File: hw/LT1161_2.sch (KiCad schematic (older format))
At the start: 7 parts, among them U501 MOSFET_DRIVER_LT1161, U502 MOSFET_IPG20N04S4L11ATMA1, U503 MOSFET_IPG20N04S4L11ATMA1

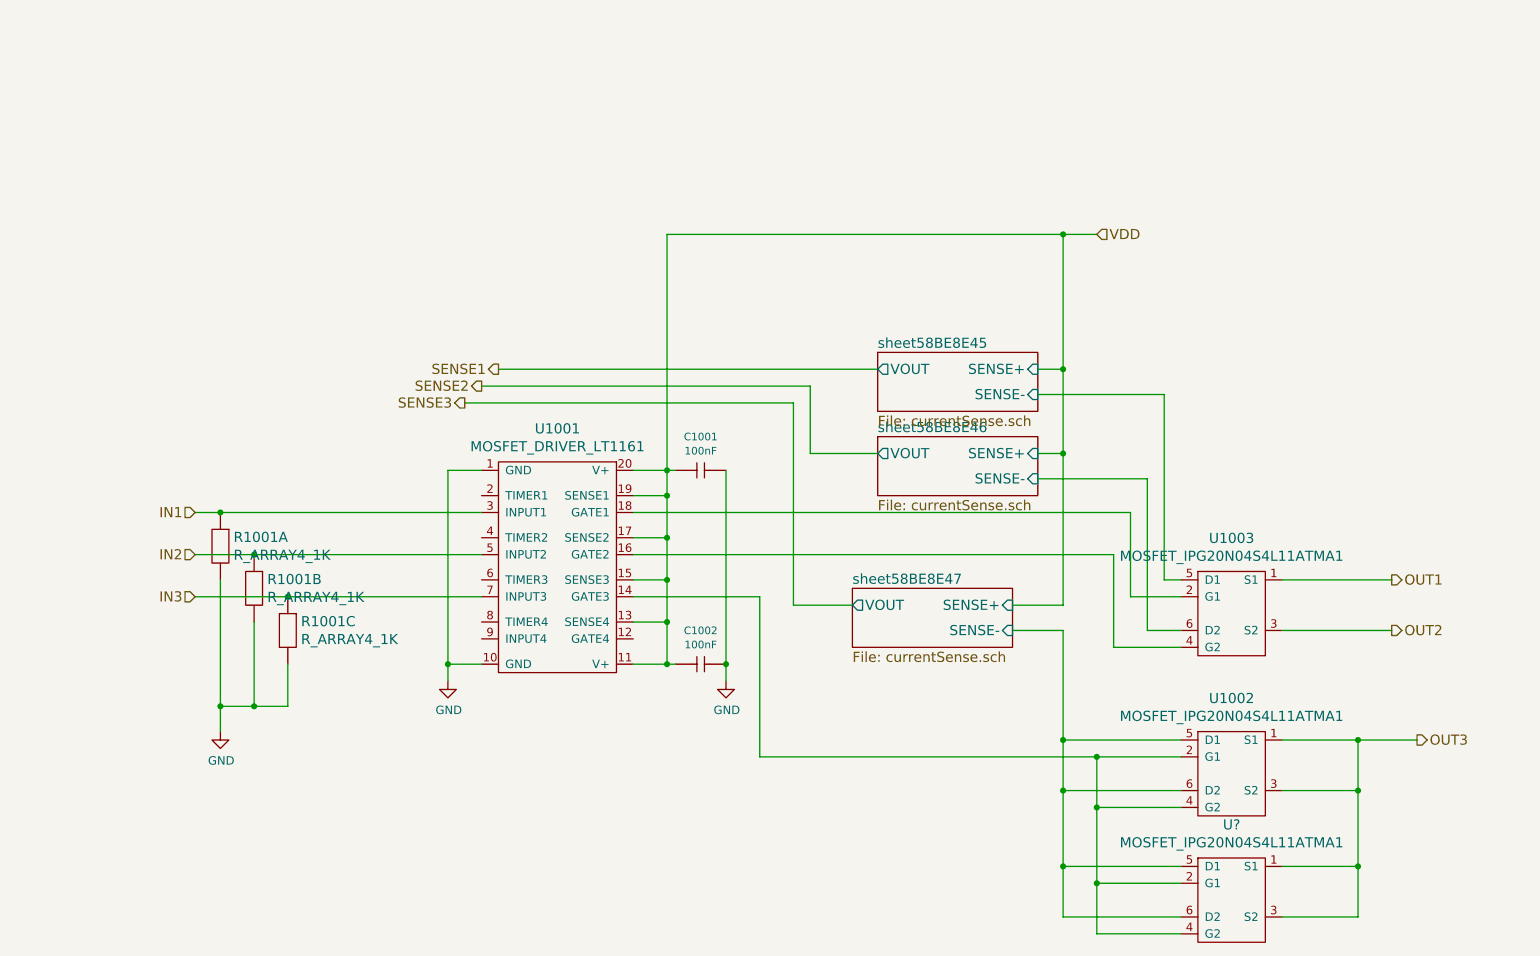
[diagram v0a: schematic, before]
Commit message: first pcb revision ready to order
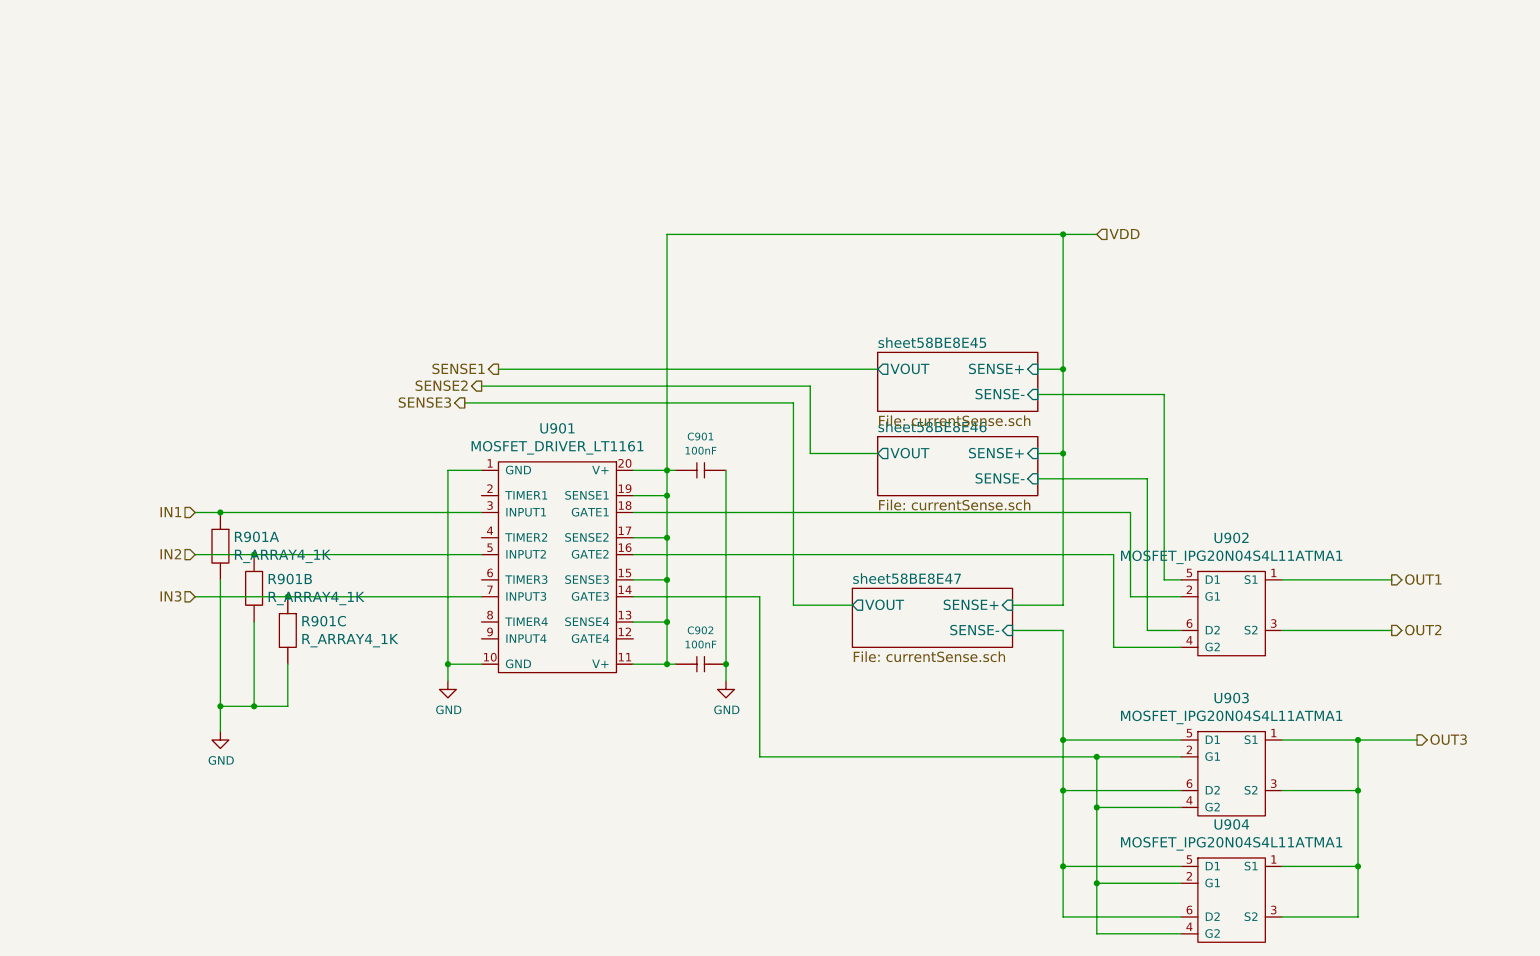
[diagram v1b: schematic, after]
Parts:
- removed C501, C502: 100nF, kemet:0603, symbol 100nF
- removed R501: R_ARRAY4_1K, usevolt:0603_array4, symbol R_ARRAY4_1K
- removed U503: MOSFET_IPG20N04S4L11ATMA1, usevolt:PG-TDSON-8-4, symbol MOSFET_IPG20N04S4L11ATMA1
- added C901, C902: 100nF, kemet:0603, symbol 100nF
- added R901: R_ARRAY4_1K, usevolt:0603_array4, symbol R_ARRAY4_1K
- added U902: MOSFET_IPG20N04S4L11ATMA1, usevolt:PG-TDSON-8-4, symbol MOSFET_IPG20N04S4L11ATMA1
- gave numbers to parts that had none: 1
- renumbered U501 to U901, U502 to U903
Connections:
- net GND: now also C901.2 (C2), C902.2 (C2), R901.2, R901.4 (2), R901.6 (2)
- net IN1: now also R901.1
- net IN2: now also R901.3 (1)
- net IN3: now also R901.5 (1)
- net OUT1: now also U902.1 (S1)
- net OUT2: now also U902.3 (S2)
- net VDD: now also C901.1 (C1), C902.1 (C1)
- net sheet58BE8E45/SENSE-: now also U902.5 (D1)
- net sheet58BE8E46/SENSE-: now also U902.6 (D2)
- net at U901.16 (GATE2): now also U902.4 (G2)
- net at U901.18 (GATE1): now also U902.2 (G1)
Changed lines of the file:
@@
 LIBS:usevolt
 LIBS:wurth_elektronik_LED
+LIBS:csb-cache
 EELAYER 26 0
 EELAYER END
@@
 $EndSheet
 $Comp
-L GND #PWR502
+L GND #PWR032
 U 1 1 58BE8E62
 P 3750 4650
-AR Path="/58BE52C9/58BE8E62" Ref="#PWR502"  Part="1"
-AR Path="/58C7B0A8/58BE8E62" Ref="#PWR1002"  Part="1"
-AR Path="/59542AAB/58BE8E62" Ref="#PWR1002"  Part="1"
-AR Path="/5954FB0E/58BE8E62" Ref="#PWR1002"  Part="1"
-F 0 "#PWR1002" H 3750 4400 50  0001 C CNN
+F 0 "#PWR032" H 3750 4400 50  0001 C CNN
 F 1 "GND" H 3755 4477 50  0000 C CNN
 F 2 "" H 3750 4650 50  0000 C CNN
@@
 $EndComp
 $Comp
-L MOSFET_DRIVER_LT1161 U501
+L MOSFET_DRIVER_LT1161 U901
 U 1 1 58BE8E74
 P 4400 3950
-AR Path="/58BE52C9/58BE8E74" Ref="U501"  Part="1"
-AR Path="/58C7B0A8/58BE8E74" Ref="U1001"  Part="1"
-AR Path="/59542AAB/58BE8E74" Ref="U1001"  Part="1"
-AR Path="/5954FB0E/58BE8E74" Ref="U1001"  Part="1"
-F 0 "U1001" H 4400 4747 60  0000 C CNN
+F 0 "U901" H 4400 4747 60  0000 C CNN
 F 1 "MOSFET_DRIVER_LT1161" H 4400 4641 60  0000 C CNN
 F 2 "usevolt:SO20" H 4450 4825 60  0001 C CNN
@@
 $Sheet
 S 6300 3200 950  350
-U 58BE8E7A
+U 595CED50
 F0 "sheet58BE8E46" 60
 F1 "currentSense.sch" 60
@@
 $Sheet
 S 6150 4100 950  350
-U 58BE8E88
+U 595CED51
 F0 "sheet58BE8E47" 60
 F1 "currentSense.sch" 60
@@
 $Comp
 L 100nF C?
-U 1 1 58BE8EAF
+U 1 1 595CED52
 P 5200 3400
-AR Path="/58BE8EAF" Ref="C?"  Part="1"
-AR Path="/58BE52C9/58BE8EAF" Ref="C501"  Part="1"
-AR Path="/58C7B0A8/58BE8EAF" Ref="C1001"  Part="1"
-AR Path="/59542AAB/58BE8EAF" Ref="C1001"  Part="1"
-AR Path="/5954FB0E/58BE8EAF" Ref="C1001"  Part="1"
-F 0 "C1001" H 5250 3599 45  0000 C CNN
+AR Path="/595CED52" Ref="C?"  Part="1"
+AR Path="/58BE52C9/595CED52" Ref="C?"  Part="1"
+AR Path="/58C7B0A8/595CED52" Ref="C?"  Part="1"
+AR Path="/59542AAB/595CED52" Ref="C?"  Part="1"
+AR Path="/5954FB0E/595CED52" Ref="C901"  Part="1"
+F 0 "C901" H 5250 3599 45  0000 C CNN
 F 1 "100nF" H 5250 3515 45  0000 C CNN
 F 2 "kemet:0603" H 5230 3550 20  0001 C CNN
@@
 $Comp
 L 100nF C?
-U 1 1 58BE8EBA
+U 1 1 595CED53
 P 5200 4550
-AR Path="/58BE8EBA" Ref="C?"  Part="1"
-AR Path="/58BE52C9/58BE8EBA" Ref="C502"  Part="1"
-AR Path="/58C7B0A8/58BE8EBA" Ref="C1002"  Part="1"
-AR Path="/59542AAB/58BE8EBA" Ref="C1002"  Part="1"
-AR Path="/5954FB0E/58BE8EBA" Ref="C1002"  Part="1"
-F 0 "C1002" H 5250 4749 45  0000 C CNN
+AR Path="/595CED53" Ref="C?"  Part="1"
+AR Path="/58BE52C9/595CED53" Ref="C?"  Part="1"
+AR Path="/58C7B0A8/595CED53" Ref="C?"  Part="1"
+AR Path="/59542AAB/595CED53" Ref="C?"  Part="1"
+AR Path="/5954FB0E/595CED53" Ref="C902"  Part="1"
+F 0 "C902" H 5250 4749 45  0000 C CNN
 F 1 "100nF" H 5250 4665 45  0000 C CNN
 F 2 "kemet:0603" H 5230 4700 20  0001 C CNN
@@
 $EndComp
 $Comp
-L GND #PWR503
+L GND #PWR033
 U 1 1 58BE8EC1
 P 5400 4650
-AR Path="/58BE52C9/58BE8EC1" Ref="#PWR503"  Part="1"
-AR Path="/58C7B0A8/58BE8EC1" Ref="#PWR1003"  Part="1"
-AR Path="/59542AAB/58BE8EC1" Ref="#PWR1003"  Part="1"
-AR Path="/5954FB0E/58BE8EC1" Ref="#PWR1003"  Part="1"
-F 0 "#PWR1003" H 5400 4400 50  0001 C CNN
+F 0 "#PWR033" H 5400 4400 50  0001 C CNN
 F 1 "GND" H 5405 4477 50  0000 C CNN
 F 2 "" H 5400 4650 50  0000 C CNN
@@
 VDD
 $Comp
-L MOSFET_IPG20N04S4L11ATMA1 U502
+L MOSFET_IPG20N04S4L11ATMA1 U903
 U 1 1 591C1D78
 P 8400 5200
-AR Path="/58BE52C9/591C1D78" Ref="U502"  Part="1"
-AR Path="/58C7B0A8/591C1D78" Ref="U1002"  Part="1"
-AR Path="/59542AAB/591C1D78" Ref="U1002"  Part="1"
-AR Path="/5954FB0E/591C1D78" Ref="U1002"  Part="1"
-F 0 "U1002" H 8400 5647 60  0000 C CNN
+F 0 "U903" H 8400 5647 60  0000 C CNN
 F 1 "MOSFET_IPG20N04S4L11ATMA1" H 8400 5541 60  0000 C CNN
 F 2 "usevolt:PG-TDSON-8-4" H 8400 5700 60  0001 C CNN
@@
 $EndComp
 $Comp
-L MOSFET_IPG20N04S4L11ATMA1 U503
-U 1 1 591C1E34
+L MOSFET_IPG20N04S4L11ATMA1 U902
+U 1 1 595CED56
 P 8400 4250
-AR Path="/58BE52C9/591C1E34" Ref="U503"  Part="1"
-AR Path="/58C7B0A8/591C1E34" Ref="U1003"  Part="1"
-AR Path="/59542AAB/591C1E34" Ref="U1003"  Part="1"
-AR Path="/5954FB0E/591C1E34" Ref="U1003"  Part="1"
-F 0 "U1003" H 8400 4697 60  0000 C CNN
+F 0 "U902" H 8400 4697 60  0000 C CNN
 F 1 "MOSFET_IPG20N04S4L11ATMA1" H 8400 4591 60  0000 C CNN
 F 2 "usevolt:PG-TDSON-8-4" H 8400 4750 60  0001 C CNN
@@
 $EndComp
 $Comp
-L R_ARRAY4_1K R501
-U 1 1 593FBF1A
+L R_ARRAY4_1K R901
+U 1 1 595CED57
 P 2400 3850
-AR Path="/58BE52C9/593FBF1A" Ref="R501"  Part="1"
-AR Path="/58C7B0A8/593FBF1A" Ref="R1001"  Part="1"
-AR Path="/59542AAB/593FBF1A" Ref="R1001"  Part="1"
-AR Path="/5954FB0E/593FBF1A" Ref="R1001"  Part="1"
-F 0 "R1001" V 2347 3928 60  0000 L CNN
+F 0 "R901" V 2347 3928 60  0000 L CNN
 F 1 "R_ARRAY4_1K" V 2453 3928 60  0000 L CNN
 F 2 "usevolt:0603_array4" H 2300 3950 60  0001 C CNN
@@
 $EndComp
 $Comp
-L R_ARRAY4_1K R501
-U 2 1 593FBFF5
+L R_ARRAY4_1K R901
+U 2 1 595CED58
 P 2600 4100
-AR Path="/58BE52C9/593FBFF5" Ref="R501"  Part="2"
-AR Path="/58C7B0A8/593FBFF5" Ref="R1001"  Part="2"
-AR Path="/59542AAB/593FBFF5" Ref="R1001"  Part="2"
-AR Path="/5954FB0E/593FBFF5" Ref="R1001"  Part="2"
-F 0 "R1001" V 2547 4178 60  0000 L CNN
+F 0 "R901" V 2547 4178 60  0000 L CNN
 F 1 "R_ARRAY4_1K" V 2653 4178 60  0000 L CNN
 F 2 "usevolt:0603_array4" H 2500 4200 60  0001 C CNN
@@
 $EndComp
 $Comp
-L R_ARRAY4_1K R501
-U 3 1 593FC0D3
+L R_ARRAY4_1K R901
+U 3 1 595CED59
 P 2800 4350
-AR Path="/58BE52C9/593FC0D3" Ref="R501"  Part="3"
-AR Path="/58C7B0A8/593FC0D3" Ref="R1001"  Part="3"
-AR Path="/59542AAB/593FC0D3" Ref="R1001"  Part="3"
-AR Path="/5954FB0E/593FC0D3" Ref="R1001"  Part="3"
-F 0 "R1001" V 2747 4428 60  0000 L CNN
+F 0 "R901" V 2747 4428 60  0000 L CNN
 F 1 "R_ARRAY4_1K" V 2853 4428 60  0000 L CNN
 F 2 "usevolt:0603_array4" H 2700 4450 60  0001 C CNN
@@
 $EndComp
 $Comp
-L GND #PWR501
-U 1 1 593FC6CE
+L GND #PWR034
+U 1 1 595CED5A
 P 2400 4950
-AR Path="/58BE52C9/593FC6CE" Ref="#PWR501"  Part="1"
-AR Path="/58C7B0A8/593FC6CE" Ref="#PWR1001"  Part="1"
-AR Path="/59542AAB/593FC6CE" Ref="#PWR1001"  Part="1"
-AR Path="/5954FB0E/593FC6CE" Ref="#PWR1001"  Part="1"
-F 0 "#PWR1001" H 2400 4700 50  0001 C CNN
+F 0 "#PWR034" H 2400 4700 50  0001 C CNN
 F 1 "GND" H 2405 4777 50  0000 C CNN
 F 2 "" H 2400 4950 50  0000 C CNN
@@
 $EndComp
 $Comp
-L MOSFET_IPG20N04S4L11ATMA1 U?
+L MOSFET_IPG20N04S4L11ATMA1 U904
 U 1 1 5955DCC6
 P 8400 5950
-F 0 "U?" H 8400 6397 60  0000 C CNN
+F 0 "U904" H 8400 6397 60  0000 C CNN
 F 1 "MOSFET_IPG20N04S4L11ATMA1" H 8400 6291 60  0000 C CNN
 F 2 "usevolt:PG-TDSON-8-4" H 8400 6450 60  0001 C CNN
@@
 	8000 4050 8100 4050
 Wire Wire Line
-	2250 3650 2400 3650
-Wire Wire Line
-	2400 3650 3950 3650
+	2250 3650 3950 3650
 Connection ~ 3750 4550
 Wire Wire Line
@@
 	3750 4550 3950 4550
 Wire Wire Line
-	3750 3400 3750 4550
-Wire Wire Line
-	3750 4550 3750 4650
+	3750 3400 3750 4650
 Connection ~ 5050 4300
 Wire Wire Line
-	4850 4550 5050 4550
-Wire Wire Line
-	5050 4550 5100 4550
+	4850 4550 5100 4550
 Connection ~ 5050 4050
 Wire Wire Line
@@
 	5050 3550 4850 3550
 Wire Wire Line
-	4850 3400 5050 3400
-Wire Wire Line
-	5050 3400 5100 3400
-Wire Wire Line
-	5050 2000 5050 3400
-Wire Wire Line
-	5050 3400 5050 3550
-Wire Wire Line
-	5050 3550 5050 3800
-Wire Wire Line
-	5050 3800 5050 4050
-Wire Wire Line
-	5050 4050 5050 4300
-Wire Wire Line
-	5050 4300 5050 4550
+	4850 3400 5100 3400
+Wire Wire Line
+	5050 2000 5050 4550
 Wire Wire Line
 	7900 4350 8100 4350
@@
 	5900 3300 6300 3300
 Wire Wire Line
-	2250 3900 2600 3900
-Wire Wire Line
-	2600 3900 3950 3900
-Wire Wire Line
-	5600 5100 7600 5100
-Wire Wire Line
-	7600 5100 8100 5100
+	2250 3900 3950 3900
+Wire Wire Line
+	5600 5100 8100 5100
 Wire Wire Line
 	5600 5100 5600 4150
@@
 	7100 4350 7400 4350
 Wire Wire Line
-	7400 4350 7400 5000
-Wire Wire Line
-	7400 5000 7400 5300
-Wire Wire Line
-	7400 5300 7400 5750
-Wire Wire Line
-	7400 5750 7400 6050
+	7400 4350 7400 6050
 Wire Wire Line
 	7400 5000 8100 5000
 Wire Wire Line
-	2250 4150 2800 4150
-Wire Wire Line
-	2800 4150 3950 4150
+	2250 4150 3950 4150
 Wire Wire Line
 	3850 3000 5800 3000
@@
 Connection ~ 5050 4550
 Wire Wire Line
-	5400 3400 5400 4550
-Wire Wire Line
-	5400 4550 5400 4650
+	5400 3400 5400 4650
 Connection ~ 5400 4550
 Wire Wire Line
-	8700 5000 9150 5000
-Wire Wire Line
-	9150 5000 9500 5000
+	8700 5000 9500 5000
 Wire Wire Line
 	8700 4350 9350 4350
@@
 	7400 2800 7250 2800
 Wire Wire Line
-	7400 2000 7400 2800
-Wire Wire Line
-	7400 2800 7400 3300
-Wire Wire Line
-	7400 3300 7400 4200
-Wire Wire Line
-	5050 2000 7400 2000
-Wire Wire Line
-	7400 2000 7600 2000
+	7400 2000 7400 4200
+Wire Wire Line
+	5050 2000 7600 2000
 Connection ~ 7400 2000
 Connection ~ 2800 4150
@@
 Connection ~ 2400 3650
 Wire Wire Line
-	2400 4050 2400 4800
-Wire Wire Line
-	2400 4800 2400 4950
+	2400 4050 2400 4950
 Wire Wire Line
 	2600 4300 2600 4800
@@
 Connection ~ 2600 4800
 Wire Wire Line
-	7600 5100 7600 5400
-Wire Wire Line
-	7600 5400 7600 5850
-Wire Wire Line
-	7600 5850 7600 6150
+	7600 5100 7600 6150
 Wire Wire Line
 	7600 5850 8100 5850
@@
 Connection ~ 7400 5000
 Wire Wire Line
-	8700 5750 9150 5750
-Wire Wire Line
-	9150 5000 9150 5300
-Wire Wire Line
-	9150 5300 9150 5750
-Wire Wire Line
-	9150 5750 9150 6050
+	9150 5750 8700 5750
+Wire Wire Line
+	9150 5000 9150 6050
 Connection ~ 9150 5000
 Connection ~ 7400 3300
 Wire Wire Line
-	2800 4800 2600 4800
-Wire Wire Line
-	2600 4800 2400 4800
+	2400 4800 2800 4800
 Wire Wire Line
 	8100 5300 7400 5300

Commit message: sw directory created, oil cooler added in hw
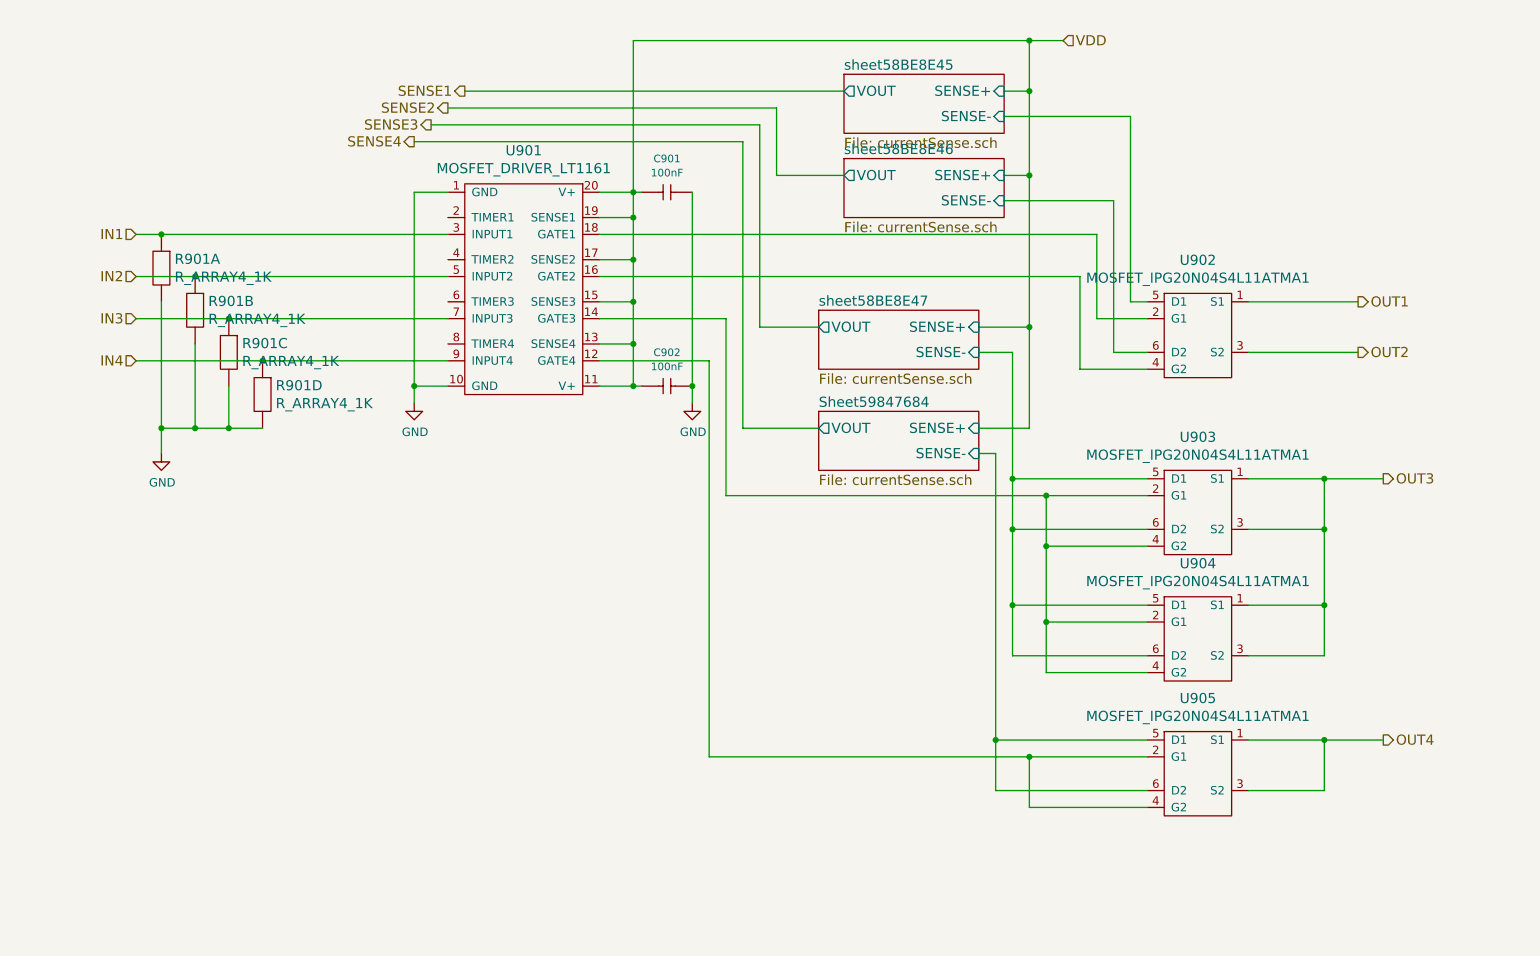
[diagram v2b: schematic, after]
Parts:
- added unit 4 of R901
- added U905: MOSFET_IPG20N04S4L11ATMA1, usevolt:PG-TDSON-8-4, symbol MOSFET_IPG20N04S4L11ATMA1
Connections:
- net GND: now also R901.8 (2)
- net at U901.12 (GATE4): now also U905.2 (G1), U905.4 (G2)
- net IN4: now reaches U901.9 (INPUT4)
- net IN4: now also R901.7 (1)
- new net OUT4: U905.1 (S1), U905.3 (S2)
- new net Sheet59847684/SENSE-: U905.5 (D1), U905.6 (D2)
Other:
- moved on the sheet: C901, C902, R901A, R901B, R901C, U901, U902, U903, U904
